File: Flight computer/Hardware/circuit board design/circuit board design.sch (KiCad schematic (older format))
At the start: 0 parts

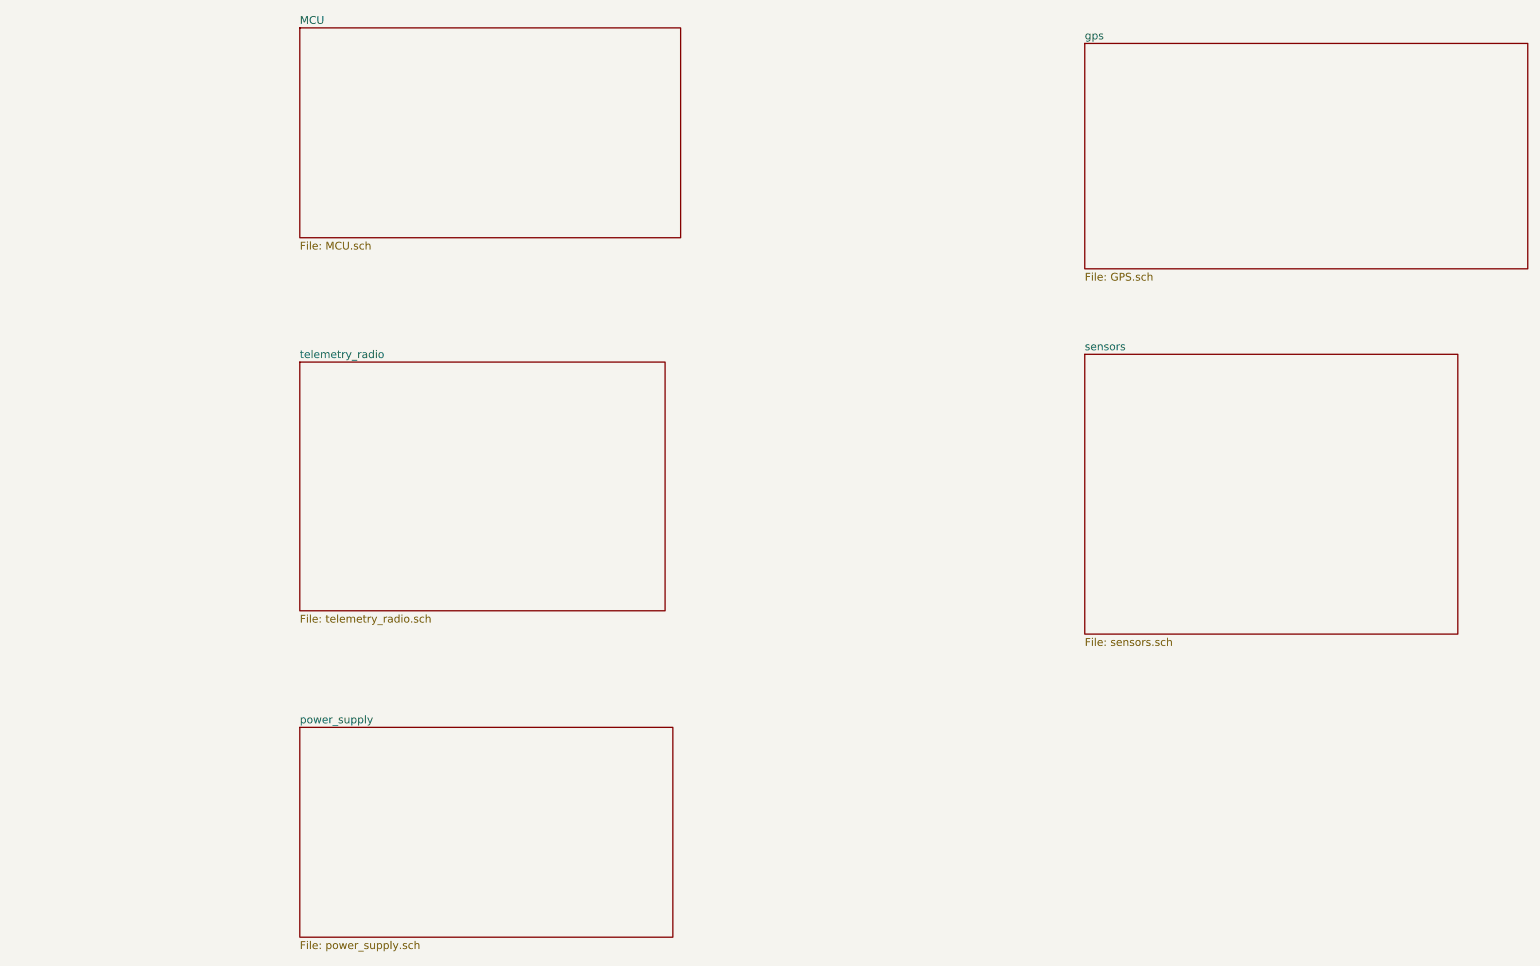
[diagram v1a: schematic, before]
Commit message: Got the GPS wired up with the MAX-M8C.
I wired up the MCU to the GPS as well. Sensors are also wired up to the I2C line.

TODO:
-make everything run on 3.3V
- work out the pyro charges and drivers
many more.
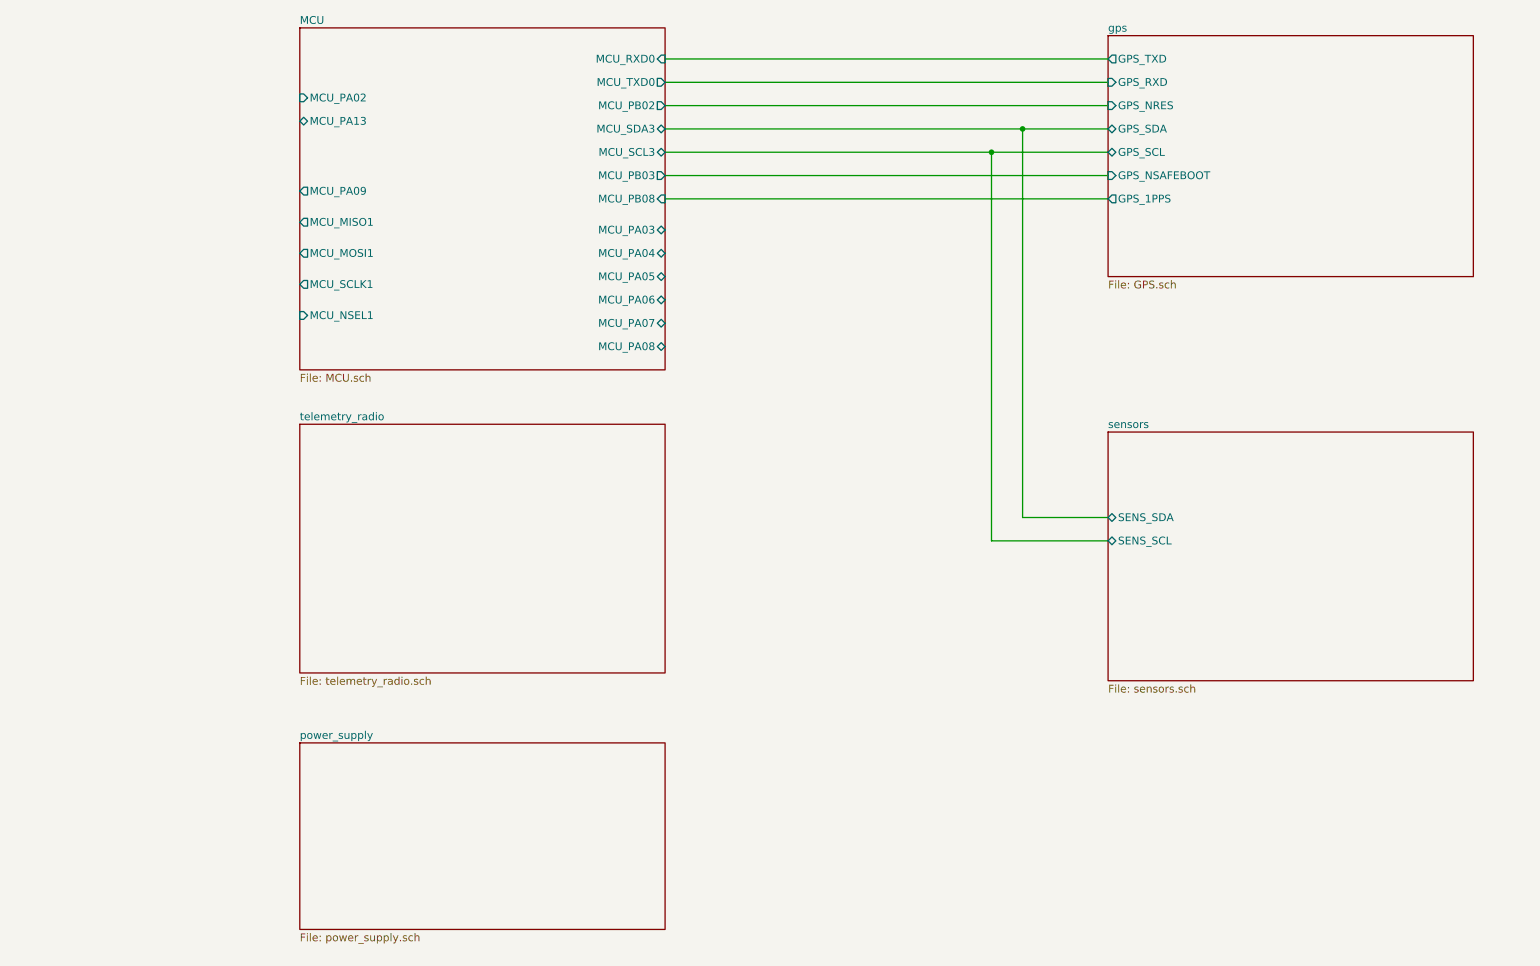
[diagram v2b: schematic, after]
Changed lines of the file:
@@
 $EndDescr
 $Sheet
-S 7750 3200 2400 1800
+S 7900 3700 2350 1600
 U 5D5B1586
 F0 "sensors" 50
 F1 "sensors.sch" 50
+F2 "SENS_SDA" B L 7900 4250 50
+F3 "SENS_SCL" B L 7900 4400 50
 $EndSheet
 $Sheet
-S 2700 1100 2450 1350
-U 5D5B15F7
-F0 "MCU" 50
-F1 "MCU.sch" 50
-$EndSheet
-$Sheet
-S 7750 1200 2850 1450
-U 5D5B165E
-F0 "gps" 50
-F1 "GPS.sch" 50
-$EndSheet
-$Sheet
-S 2700 5600 2400 1350
+S 2700 5700 2350 1200
 U 5D5B1705
 F0 "power_supply" 50
@@
 $EndSheet
 $Sheet
-S 2700 3250 2350 1600
+S 2700 3650 2350 1600
 U 5D5B17D8
 F0 "telemetry_radio" 50
 F1 "telemetry_radio.sch" 50
 $EndSheet
+$Sheet
+S 7900 1150 2350 1550
+U 5D5B165E
+F0 "gps" 50
+F1 "GPS.sch" 50
+F2 "GPS_SCL" B L 7900 1900 50
+F3 "GPS_SDA" B L 7900 1750 50
+F4 "GPS_TXD" O L 7900 1300 50
+F5 "GPS_RXD" I L 7900 1450 50
+F6 "GPS_NSAFEBOOT" I L 7900 2050 50
+F7 "GPS_NRES" I L 7900 1600 50
+F8 "GPS_1PPS" O L 7900 2200 50
+$EndSheet
+Wire Wire Line
+	7900 4250 7350 4250
+Wire Wire Line
+	7900 4400 7150 4400
+Wire Wire Line
+	7900 1300 5050 1300
+Wire Wire Line
+	5050 1450 7900 1450
+$Sheet
+S 2700 1100 2350 2200
+U 5D5B15F7
+F0 "MCU" 50
+F1 "MCU.sch" 50
+F2 "MCU_MOSI1" O L 2700 2550 50
+F3 "MCU_SCLK1" O L 2700 2750 50
+F4 "MCU_NSEL1" I L 2700 2950 50
+F5 "MCU_MISO1" O L 2700 2350 50
+F6 "MCU_SDA3" B R 5050 1750 50
+F7 "MCU_SCL3" B R 5050 1900 50
+F8 "MCU_TXD0" O R 5050 1450 50
+F9 "MCU_RXD0" I R 5050 1300 50
+F10 "MCU_PA02" I L 2700 1550 50
+F11 "MCU_PA03" B R 5050 2400 50
+F12 "MCU_PA04" B R 5050 2550 50
+F13 "MCU_PA05" B R 5050 2700 50
+F14 "MCU_PA06" B R 5050 2850 50
+F15 "MCU_PA07" B R 5050 3000 50
+F16 "MCU_PA08" B R 5050 3150 50
+F17 "MCU_PA09" O L 2700 2150 50
+F18 "MCU_PA13" B L 2700 1700 50
+F19 "MCU_PB03" O R 5050 2050 50
+F20 "MCU_PB02" O R 5050 1600 50
+F21 "MCU_PB08" I R 5050 2200 50
+$EndSheet
+Wire Wire Line
+	5050 1750 7350 1750
+Wire Wire Line
+	5050 1900 7150 1900
+Wire Wire Line
+	7350 4250 7350 1750
+Connection ~ 7350 1750
+Wire Wire Line
+	7350 1750 7900 1750
+Wire Wire Line
+	7150 4400 7150 1900
+Connection ~ 7150 1900
+Wire Wire Line
+	7150 1900 7900 1900
+Wire Wire Line
+	5050 2050 7900 2050
+Wire Wire Line
+	7900 2200 5050 2200
+Wire Wire Line
+	5050 1600 7900 1600
 $EndSCHEMATC

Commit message: changed boost converter resistor values for 3.3V and more
-started the pyro drivers
- connected the SPI connection between radio and MCU
- boost converter values changed.
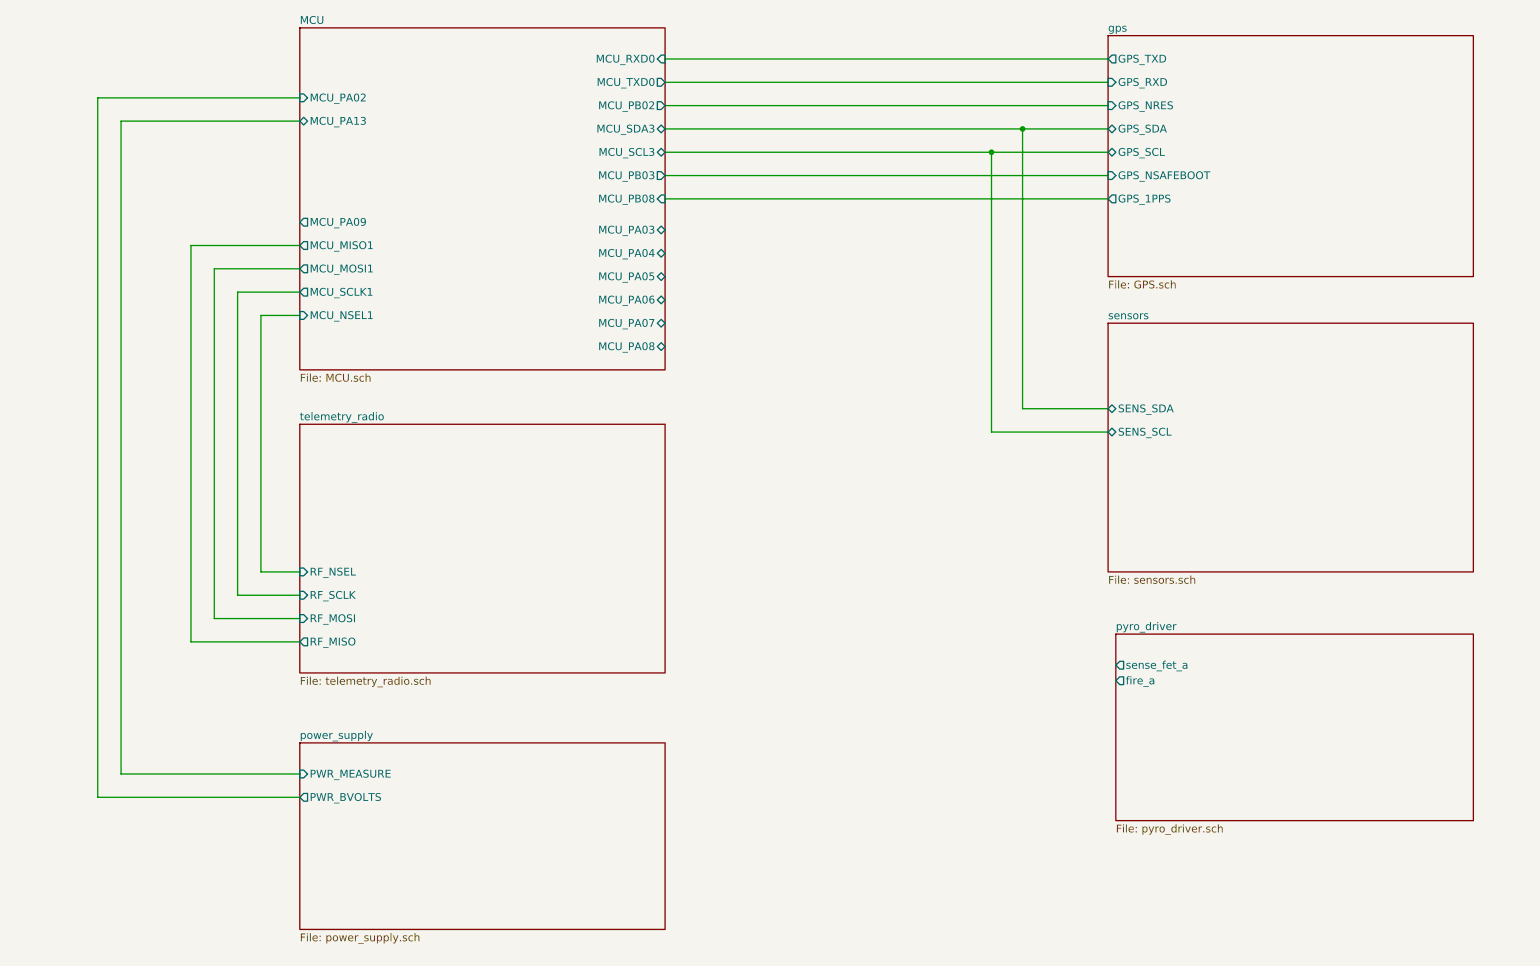
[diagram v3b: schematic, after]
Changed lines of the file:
@@
 $Descr A4 11693 8268
 encoding utf-8
-Sheet 1 6
+Sheet 1 7
 Title "flight computer for rocket"
 Date "2019-08-19"
@@
 $EndDescr
 $Sheet
-S 7900 3700 2350 1600
+S 7900 3000 2350 1600
 U 5D5B1586
 F0 "sensors" 50
 F1 "sensors.sch" 50
-F2 "SENS_SDA" B L 7900 4250 50
-F3 "SENS_SCL" B L 7900 4400 50
+F2 "SENS_SDA" B L 7900 3550 50
+F3 "SENS_SCL" B L 7900 3700 50
 $EndSheet
 $Sheet
@@
 F0 "power_supply" 50
 F1 "power_supply.sch" 50
+F2 "PWR_BVOLTS" O L 2700 6050 50
+F3 "PWR_MEASURE" I L 2700 5900 50
 $EndSheet
 $Sheet
@@
 F0 "telemetry_radio" 50
 F1 "telemetry_radio.sch" 50
+F2 "RF_SCLK" I L 2700 4750 50
+F3 "RF_MISO" O L 2700 5050 50
+F4 "RF_MOSI" I L 2700 4900 50
+F5 "RF_NSEL" I L 2700 4600 50
 $EndSheet
 $Sheet
@@
 $EndSheet
 Wire Wire Line
-	7900 4250 7350 4250
+	7900 3550 7350 3550
 Wire Wire Line
-	7900 4400 7150 4400
+	7900 3700 7150 3700
 Wire Wire Line
 	7900 1300 5050 1300
@@
 F0 "MCU" 50
 F1 "MCU.sch" 50
-F2 "MCU_MOSI1" O L 2700 2550 50
-F3 "MCU_SCLK1" O L 2700 2750 50
+F2 "MCU_MOSI1" O L 2700 2650 50
+F3 "MCU_SCLK1" O L 2700 2800 50
 F4 "MCU_NSEL1" I L 2700 2950 50
-F5 "MCU_MISO1" O L 2700 2350 50
+F5 "MCU_MISO1" O L 2700 2500 50
 F6 "MCU_SDA3" B R 5050 1750 50
 F7 "MCU_SCL3" B R 5050 1900 50
@@
 F15 "MCU_PA07" B R 5050 3000 50
 F16 "MCU_PA08" B R 5050 3150 50
-F17 "MCU_PA09" O L 2700 2150 50
+F17 "MCU_PA09" O L 2700 2350 50
 F18 "MCU_PA13" B L 2700 1700 50
 F19 "MCU_PB03" O R 5050 2050 50
@@
 	5050 1900 7150 1900
 Wire Wire Line
-	7350 4250 7350 1750
+	7350 3550 7350 1750
 Connection ~ 7350 1750
 Wire Wire Line
 	7350 1750 7900 1750
 Wire Wire Line
-	7150 4400 7150 1900
+	7150 3700 7150 1900
 Connection ~ 7150 1900
 Wire Wire Line
@@
 Wire Wire Line
 	5050 1600 7900 1600
+$Sheet
+S 7950 5000 2300 1200
+U 5D6468D5
+F0 "pyro_driver" 50
+F1 "pyro_driver.sch" 50
+F2 "sense_fet_a" O L 7950 5200 50
+F3 "fire_a" O L 7950 5300 50
+$EndSheet
+Wire Wire Line
+	2700 1550 1400 1550
+Wire Wire Line
+	1400 1550 1400 6050
+Wire Wire Line
+	1400 6050 2700 6050
+Wire Wire Line
+	2700 1700 1550 1700
+Wire Wire Line
+	1550 1700 1550 5900
+Wire Wire Line
+	1550 5900 2700 5900
+Wire Wire Line
+	2700 5050 2000 5050
+Wire Wire Line
+	2000 5050 2000 2500
+Wire Wire Line
+	2000 2500 2700 2500
+Wire Wire Line
+	2700 4900 2150 4900
+Wire Wire Line
+	2150 4900 2150 2650
+Wire Wire Line
+	2150 2650 2700 2650
+Wire Wire Line
+	2700 4750 2300 4750
+Wire Wire Line
+	2300 4750 2300 2800
+Wire Wire Line
+	2300 2800 2700 2800
+Wire Wire Line
+	2700 2950 2450 2950
+Wire Wire Line
+	2450 2950 2450 4600
+Wire Wire Line
+	2450 4600 2700 4600
 $EndSCHEMATC

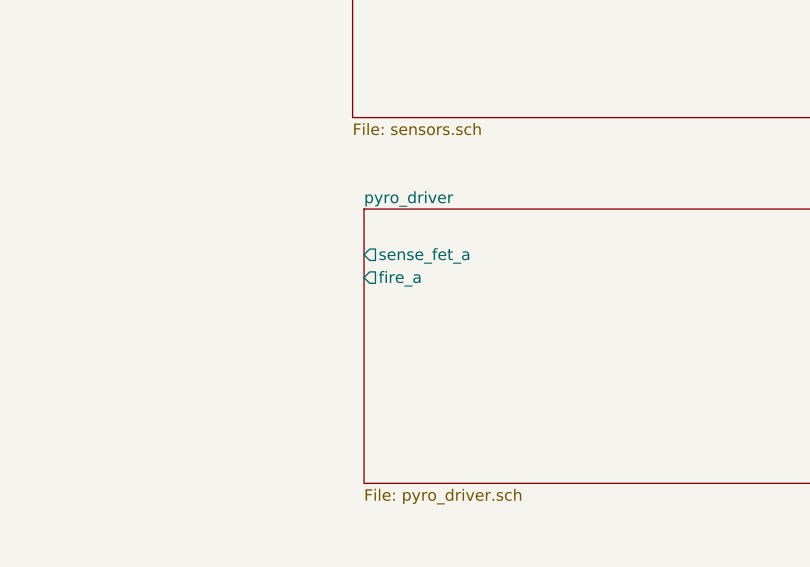
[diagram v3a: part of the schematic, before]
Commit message: Wired up the SI4463 according to AN628 figure 16. Component values have not been set. Only type of component.
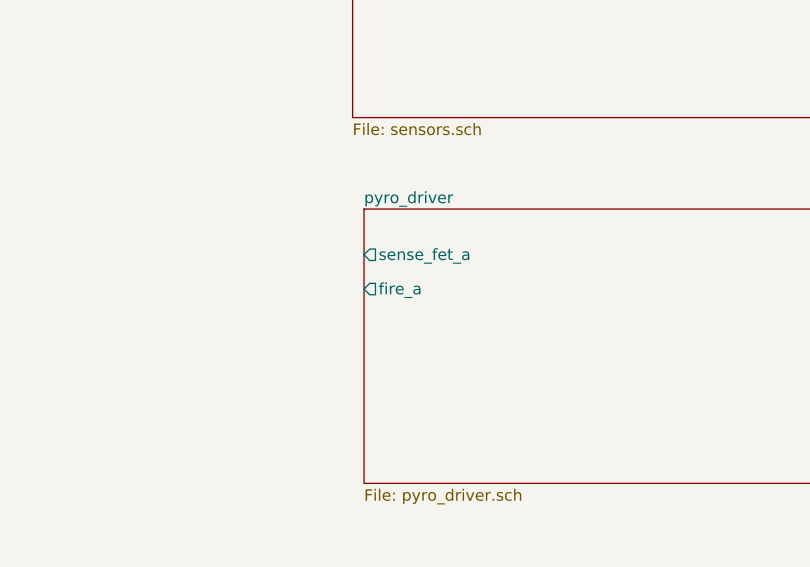
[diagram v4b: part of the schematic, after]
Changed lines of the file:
@@
 F1 "pyro_driver.sch" 50
 F2 "sense_fet_a" O L 7950 5200 50
-F3 "fire_a" O L 7950 5300 50
+F3 "fire_a" O L 7950 5350 50
 $EndSheet
 Wire Wire Line

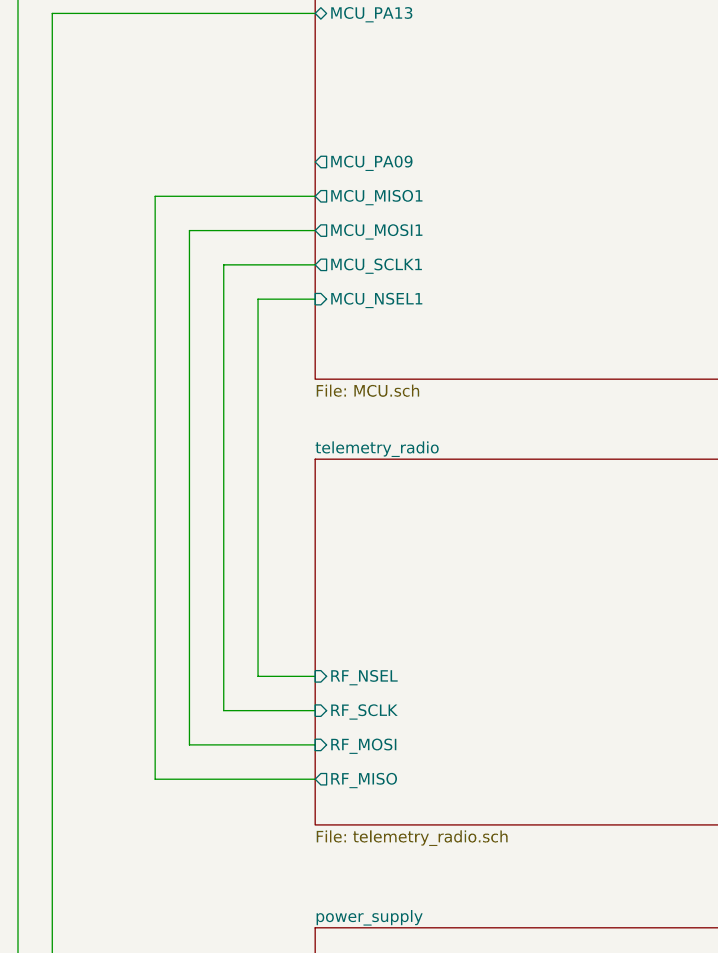
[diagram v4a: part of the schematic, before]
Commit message: Swapped out the XTAL with a tcxo for radio.
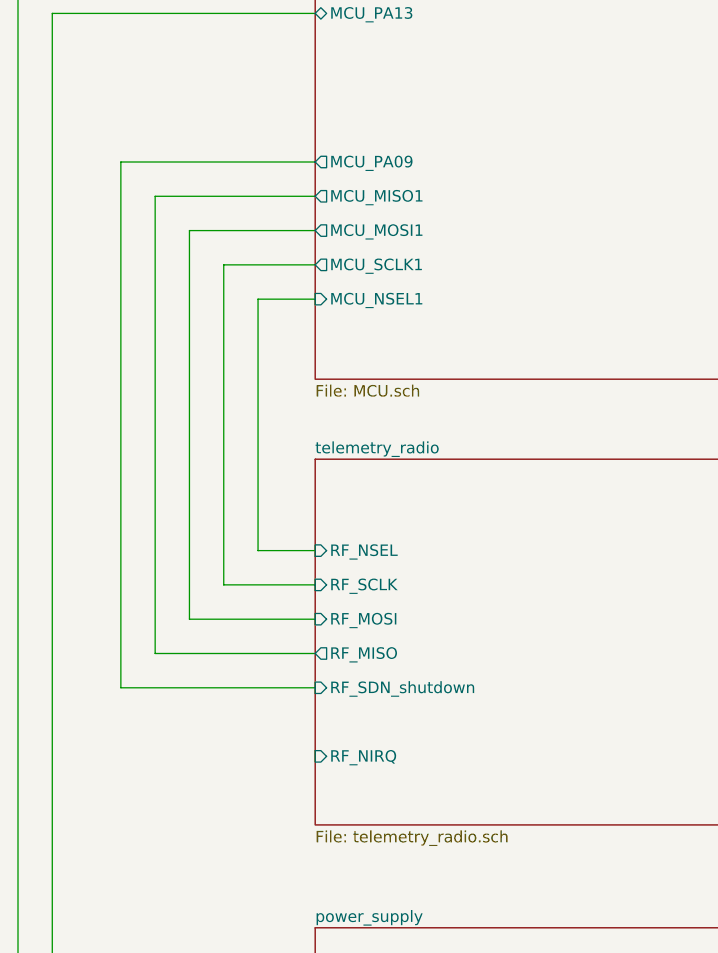
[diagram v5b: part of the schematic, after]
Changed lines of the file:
@@
-$EndSheet
-$Sheet
-S 2700 3650 2350 1600
-U 5D5B17D8
-F0 "telemetry_radio" 50
-F1 "telemetry_radio.sch" 50
-F2 "RF_SCLK" I L 2700 4750 50
-F3 "RF_MISO" O L 2700 5050 50
-F4 "RF_MOSI" I L 2700 4900 50
-F5 "RF_NSEL" I L 2700 4600 50
 $EndSheet
 $Sheet
@@
 	1550 5900 2700 5900
 Wire Wire Line
-	2700 5050 2000 5050
-Wire Wire Line
-	2000 5050 2000 2500
-Wire Wire Line
 	2000 2500 2700 2500
 Wire Wire Line
-	2700 4900 2150 4900
-Wire Wire Line
-	2150 4900 2150 2650
-Wire Wire Line
 	2150 2650 2700 2650
-Wire Wire Line
-	2700 4750 2300 4750
-Wire Wire Line
-	2300 4750 2300 2800
 Wire Wire Line
 	2300 2800 2700 2800
@@
 	2700 2950 2450 2950
 Wire Wire Line
-	2450 2950 2450 4600
+	2450 4050 2700 4050
 Wire Wire Line
-	2450 4600 2700 4600
+	2700 4350 2150 4350
+Wire Wire Line
+	2700 4500 2000 4500
+Wire Wire Line
+	2700 4200 2300 4200
+Wire Wire Line
+	2300 4200 2300 2800
+Wire Wire Line
+	2150 4350 2150 2650
+Wire Wire Line
+	2000 4500 2000 2500
+Wire Wire Line
+	2450 2950 2450 4050
+$Sheet
+S 2700 3650 2350 1600
+U 5D5B17D8
+F0 "telemetry_radio" 50
+F1 "telemetry_radio.sch" 50
+F2 "RF_SCLK" I L 2700 4200 50
+F3 "RF_MISO" O L 2700 4500 50
+F4 "RF_MOSI" I L 2700 4350 50
+F5 "RF_NSEL" I L 2700 4050 50
+F6 "RF_SDN_shutdown" I L 2700 4650 50
+F7 "RF_NIRQ" I L 2700 4950 50
+$EndSheet
+Wire Wire Line
+	2700 4650 1850 4650
+Wire Wire Line
+	1850 2350 2700 2350
+Wire Wire Line
+	1850 2350 1850 4650
 $EndSCHEMATC
